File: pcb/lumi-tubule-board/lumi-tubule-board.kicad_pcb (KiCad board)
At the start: 2 copper layers, 66 parts, among them Q1 DMN1045UFR4, SW1 SWITCH_TACT_SMT4.6X2.8, SW2 SWITCH_TACT_SMT4.6X2.8, U1 SHTC3, U2 VREG_SOT23-5, U3 ESP32-S3-MINI-1, X1 USB_C

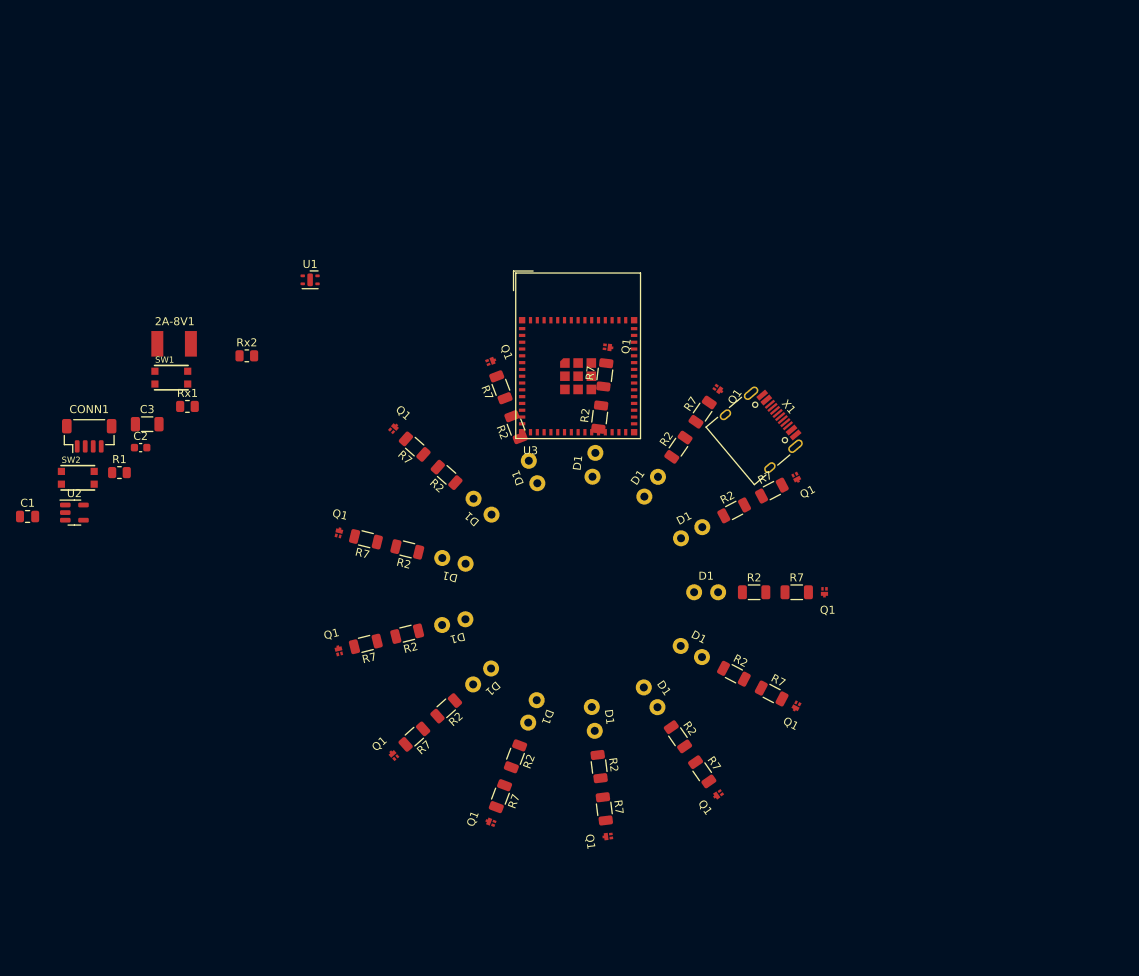
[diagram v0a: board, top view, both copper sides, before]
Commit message: PCB design update
Added LIS2DH12 accelerometer to PCB. Reworked the filament pads. Fixed footprints. Added pullup resistors to I2C lines. Started planning the layout in more compact footprint.
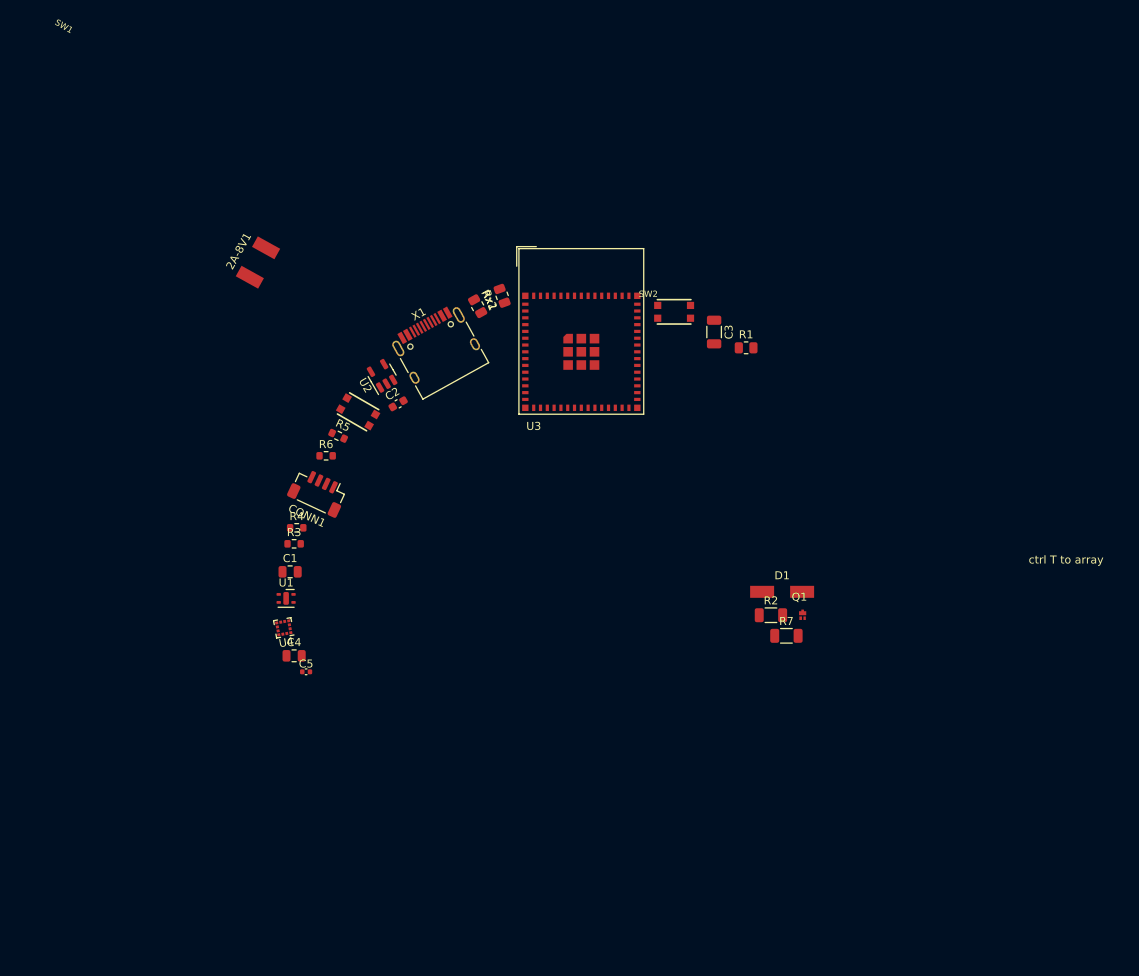
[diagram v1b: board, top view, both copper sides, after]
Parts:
- removed the D1 at (138.0, 110.6)
- removed the D1 at (166.0, 100.1)
- removed the D1 at (134.5, 96.1)
- removed the D1 at (159.1, 86.9)
- removed the D1 at (164.2, 107.5)
- removed the D1 at (164.2, 92.6)
- removed the D1 at (134.5, 103.8)
- removed the D1 at (138.1, 89.4)
- removed the D1 at (144.3, 114.9)
- removed the D1 at (151.9, 115.9)
- removed the D1 at (152.0, 84.1)
- removed the D1 at (144.4, 85.0)
- removed the D1 at (159.1, 113.2)
- removed the Q1 at (126.9, 79.6)
- removed the Q1 at (177.3, 85.7)
- removed the Q1 at (139.1, 71.2)
- removed the Q1 at (139.1, 128.8)
- removed the Q1 at (120.1, 107.4)
- removed the Q1 at (177.3, 114.3)
- removed the Q1 at (153.8, 130.6)
- removed the Q1 at (167.5, 74.7)
- removed the Q1 at (120.1, 92.7)
- removed the Q1 at (153.7, 69.4)
- removed the Q1 at (167.5, 125.3)
- removed the Q1 at (127.0, 120.4)
- removed the Q1 at (180.8, 100.0)
- removed the R2 at (172.0, 100.1)
- removed the R2 at (142.2, 79.4)
- removed the R2 at (128.6, 105.2)
- removed the R2 at (152.6, 121.8)
- removed the R2 at (162.5, 81.9)
- removed the R2 at (133.5, 114.6)
- removed the R2 at (152.7, 78.2)
- removed the R2 at (133.6, 85.4)
- removed the R2 at (142.2, 120.6)
- removed the R2 at (162.5, 118.1)
- removed the R2 at (169.5, 89.8)
- removed the R2 at (128.6, 94.7)
- removed the R2 at (169.5, 110.2)
- removed the R7 at (174.2, 112.7)
- removed the R7 at (129.6, 81.9)
- removed the R7 at (140.3, 74.4)
- removed the R7 at (140.3, 125.5)
- removed the R7 at (165.5, 122.5)
- removed the R7 at (153.3, 72.9)
- removed the R7 at (153.3, 127.1)
- removed the R7 at (177.3, 100.1)
- removed the R7 at (123.5, 106.5)
- removed the R7 at (174.2, 87.3)
- removed the R7 at (129.5, 118.1)
- removed the R7 at (123.5, 93.4)
- removed the R7 at (165.6, 77.5)
- added C4: 10uF, Capacitor_SMD:C_0805_2012Metric, F.Cu at (114.5, 108.0)
- added C5: 100nF, Capacitor_SMD:C_0402_1005Metric, F.Cu at (116.0, 110.0)
- added D1: flexible-led-filament, lumi-tubule-board:Flexible LED filament viamount, F.Cu at (175.5, 100.0)
- added Q1: DMN1045UFR4, lumi-tubule-board:DMN1045UFR4, F.Cu at (178.1, 102.9)
- added R2: 10k, Resistor_SMD:R_1206_3216Metric, F.Cu at (174.1, 102.9)
- added R3: 4.7K, Resistor_SMD:R_0603_1608Metric, F.Cu at (114.5, 94.0)
- added R4: 4.7K, Resistor_SMD:R_0603_1608Metric, F.Cu at (114.8, 92.0)
- added R5: 4.7K, Resistor_SMD:R_0603_1608Metric, F.Cu at (120.0, 80.5)
- added R6: 4.7K, Resistor_SMD:R_0603_1608Metric, F.Cu at (118.5, 83.0)
- added R7: 18, Resistor_SMD:R_1206_3216Metric, F.Cu at (176.0, 105.5)
- added U4: LIS2Dx12, Package_LGA:LGA-12_2x2mm_P0.5mm, F.Cu at (113.2, 104.5)
- moved R1 79.9 mm to (171.0, 69.5)
- moved SW2 77.4 mm to (162.0, 65.0)
- moved C3 71.8 mm to (167.0, 67.5), turned to -90 degrees
- moved U2 42.1 mm to (125.5, 73.0), turned to 120 degrees
- moved Rx1 41.7 mm to (140.5, 63.0), turned to 110 degrees
- moved X1 40.5 mm to (132.8, 70.2), turned to 29 degrees
- moved U1 39.9 mm to (113.5, 100.8)
- moved C1 33.5 mm to (114.0, 97.5)
- moved C2 32.6 mm to (127.5, 76.5), turned to 30 degrees
- moved Rx2 29.5 mm to (137.4, 64.3), turned to -61 degrees
- moved CONN1 29.5 mm to (117.5, 87.5), turned to 155 degrees
- moved SW1 23.7 mm to (122.5, 77.5), turned to -30 degrees
- moved 2A-8V1 14.6 mm to (110.0, 58.8), turned to 61 degrees
- moved U3 3.08 mm to (150.4, 67.5)
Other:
- board text added: "ctrl T to array"

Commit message: First wiring for PCB
First fully wired up arrangement for PCB. It's not pretty and the differential pairs are not good yet and the schematic still needs updating.
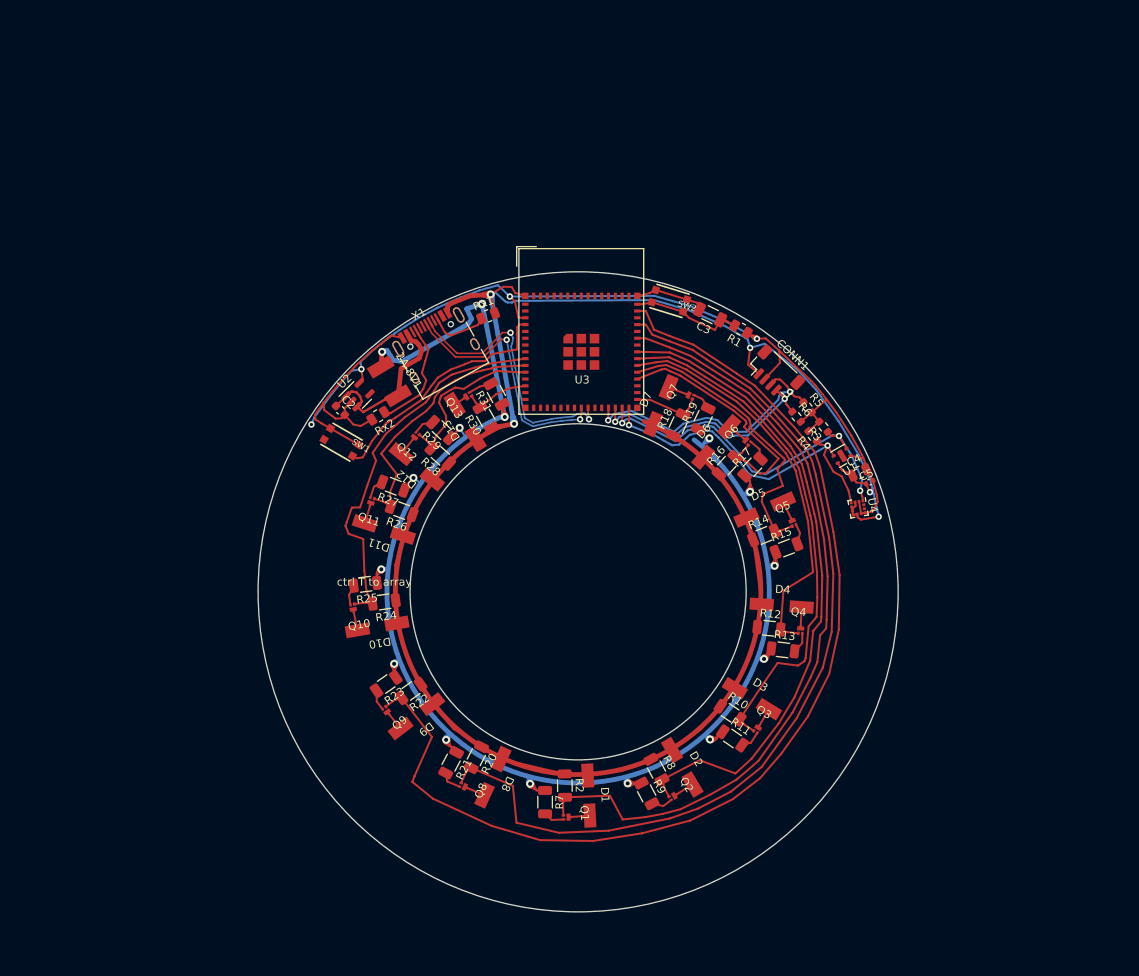
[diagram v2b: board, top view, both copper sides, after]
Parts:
- removed C1: 100nF, Capacitor_SMD:C_0805_2012Metric
- added D10: flexible-led-filament, lumi-tubule-board:Flexible LED filament viamount, F.Cu at (124.9, 104.4)
- added D11: flexible-led-filament, lumi-tubule-board:Flexible LED filament viamount, F.Cu at (125.7, 92.2)
- added D12: flexible-led-filament, lumi-tubule-board:Flexible LED filament viamount, F.Cu at (129.8, 84.4)
- added D13: flexible-led-filament, lumi-tubule-board:Flexible LED filament viamount, F.Cu at (135.9, 78.8)
- added D2: flexible-led-filament, lumi-tubule-board:Flexible LED filament viamount, F.Cu at (163.0, 121.9)
- added D3: flexible-led-filament, lumi-tubule-board:Flexible LED filament viamount, F.Cu at (171.7, 113.4)
- added D4: flexible-led-filament, lumi-tubule-board:Flexible LED filament viamount, F.Cu at (175.4, 101.7)
- added D5: flexible-led-filament, lumi-tubule-board:Flexible LED filament viamount, F.Cu at (173.3, 89.7)
- added D6: flexible-led-filament, lumi-tubule-board:Flexible LED filament viamount, F.Cu at (167.3, 81.3)
- added D7: flexible-led-filament, lumi-tubule-board:Flexible LED filament viamount, F.Cu at (160.3, 76.7)
- added D8: flexible-led-filament, lumi-tubule-board:Flexible LED filament viamount, F.Cu at (139.3, 123.2)
- added D9: flexible-led-filament, lumi-tubule-board:Flexible LED filament viamount, F.Cu at (129.8, 115.6)
- added Q10: DMN1045UFR4, lumi-tubule-board:DMN1045UFR4, F.Cu at (121.9, 101.9)
- added Q11: DMN1045UFR4, lumi-tubule-board:DMN1045UFR4, F.Cu at (124.2, 88.6)
- added Q12: DMN1045UFR4, lumi-tubule-board:DMN1045UFR4, F.Cu at (129.7, 80.5)
- added Q13: DMN1045UFR4, lumi-tubule-board:DMN1045UFR4, F.Cu at (136.2, 75.5)
- added Q2: DMN1045UFR4, lumi-tubule-board:DMN1045UFR4, F.Cu at (161.8, 125.6)
- added Q3: DMN1045UFR4, lumi-tubule-board:DMN1045UFR4, F.Cu at (172.4, 117.2)
- added Q4: DMN1045UFR4, lumi-tubule-board:DMN1045UFR4, F.Cu at (177.8, 104.8)
- added Q5: DMN1045UFR4, lumi-tubule-board:DMN1045UFR4, F.Cu at (176.9, 91.4)
- added Q6: DMN1045UFR4, lumi-tubule-board:DMN1045UFR4, F.Cu at (171.2, 81.2)
- added Q7: DMN1045UFR4, lumi-tubule-board:DMN1045UFR4, F.Cu at (164.0, 75.5)
- added Q8: DMN1045UFR4, lumi-tubule-board:DMN1045UFR4, F.Cu at (135.6, 124.3)
- added Q9: DMN1045UFR4, lumi-tubule-board:DMN1045UFR4, F.Cu at (126.0, 114.8)
- added R10: 10k, Resistor_SMD:R_1206_3216Metric, F.Cu at (169.0, 115.1)
- added R11: 18, Resistor_SMD:R_1206_3216Metric, F.Cu at (169.3, 118.3)
- added R12: 10k, Resistor_SMD:R_1206_3216Metric, F.Cu at (173.8, 104.6)
- added R13: 18, Resistor_SMD:R_1206_3216Metric, F.Cu at (175.6, 107.3)
- added R14: 10k, Resistor_SMD:R_1206_3216Metric, F.Cu at (173.2, 92.9)
- added R15: 18, Resistor_SMD:R_1206_3216Metric, F.Cu at (176.0, 94.5)
- added R16: 10k, Resistor_SMD:R_1206_3216Metric, F.Cu at (168.6, 84.2)
- added R17: 18, Resistor_SMD:R_1206_3216Metric, F.Cu at (171.8, 84.4)
- added R18: 10k, Resistor_SMD:R_1206_3216Metric, F.Cu at (162.5, 79.2)
- added R19: 18, Resistor_SMD:R_1206_3216Metric, F.Cu at (165.6, 78.4)
- added R20: 10k, Resistor_SMD:R_1206_3216Metric, F.Cu at (137.3, 120.7)
- added R21: 18, Resistor_SMD:R_1206_3216Metric, F.Cu at (134.1, 121.4)
- added R22: 10k, Resistor_SMD:R_1206_3216Metric, F.Cu at (129.1, 112.4)
- added R23: 18, Resistor_SMD:R_1206_3216Metric, F.Cu at (126.0, 111.5)
- added R24: 10k, Resistor_SMD:R_1206_3216Metric, F.Cu at (125.8, 101.3)
- added R25: 18, Resistor_SMD:R_1206_3216Metric, F.Cu at (123.4, 99.1)
- added R26: 10k, Resistor_SMD:R_1206_3216Metric, F.Cu at (127.9, 89.8)
- added R27: 18, Resistor_SMD:R_1206_3216Metric, F.Cu at (126.9, 86.8)
- added R28: 10k, Resistor_SMD:R_1206_3216Metric, F.Cu at (132.8, 83.0)
- added R29: 18, Resistor_SMD:R_1206_3216Metric, F.Cu at (132.9, 79.8)
- added R30: 10k, Resistor_SMD:R_1206_3216Metric, F.Cu at (138.5, 78.2)
- added R31: 18, Resistor_SMD:R_1206_3216Metric, F.Cu at (139.8, 75.3)
- added R8: 10k, Resistor_SMD:R_1206_3216Metric, F.Cu at (159.8, 122.2)
- added R9: 18, Resistor_SMD:R_1206_3216Metric, F.Cu at (158.6, 125.2)
- moved C5 74.3 mm to (186.4, 86.3), turned to 24 degrees
- moved C4 74.3 mm to (185.2, 85.1), turned to 24 degrees
- moved U4 73.3 mm to (185.0, 89.5), turned to -80 degrees
- moved U1 71.7 mm to (183.0, 83.0), turned to -150 degrees
- moved R3 67.8 mm to (180.7, 79.4), turned to 130 degrees
- moved R4 65.5 mm to (179.3, 80.5), turned to 130 degrees
- moved R6 59.0 mm to (177.3, 78.1), turned to -50 degrees
- moved CONN1 58.9 mm to (174.6, 72.8), turned to -43 degrees
- moved R5 58.8 mm to (178.7, 76.9), turned to -51 degrees
- moved Q1 38.8 mm to (148.5, 128.2), turned to 93 degrees
- moved R7 36.6 mm to (145.9, 126.3), turned to -90 degrees
- moved D1 35.1 mm to (151.3, 125.5), turned to -87 degrees
- moved R2 33.4 mm to (148.3, 124.2), turned to -89 degrees
- moved 2A-8V1 22.2 mm to (126.4, 73.7), turned to -59 degrees
- moved Rx2 18.5 mm to (125.0, 78.0), turned to -149 degrees
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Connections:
- CONN1 pad 1: unconnected-(CONN1-Pad1) -> GND
- CONN1 pad 2: unconnected-(CONN1-Pad2) -> /3.3V
- CONN1 pad 3: unconnected-(CONN1-Pad3) -> SDA
- CONN1 pad 4: unconnected-(CONN1-Pad4) -> SCL
- Q1 pad 2: L1 -> L7
- R2 pad 2: L1 -> L7
- U3 pad 10: L6 -> L11
- U3 pad 11: L7 -> L12
- U3 pad 12: L8 -> (no net)
- U3 pad 13: L9 -> L13
- U3 pad 14: L10 -> (no net)
- U3 pad 15: L11 -> (no net)
- U3 pad 16: L12 -> (no net)
- U3 pad 17: L13 -> (no net)
- U3 pad 27: SDA_int -> SDA
- U3 pad 28: unconnected-(U3-Pad28) -> SCL
- U3 pad 29: unconnected-(U3-Pad29) -> SCL_int
- U3 pad 30: SCL_int -> SDA_int
- U3 pad 31: unconnected-(U3-Pad31) -> L1
- U3 pad 32: unconnected-(U3-Pad32) -> (no net)
- U3 pad 33: unconnected-(U3-Pad33) -> (no net)
- U3 pad 34: unconnected-(U3-Pad34) -> L2
- U3 pad 35: unconnected-(U3-Pad35) -> L3
- U3 pad 36: unconnected-(U3-Pad36) -> L4
- U3 pad 37: unconnected-(U3-Pad37) -> L5
- U3 pad 38: unconnected-(U3-Pad38) -> L6
- U3 pad 39: unconnected-(U3-Pad39) -> (no net)
- U3 pad 40: unconnected-(U3-Pad40) -> L7
- U3 pad 42: Net-(U3-Pad1) -> L8
- U3 pad 44: unconnected-(U3-Pad44) -> L9
- U3 pad 5: L1 -> (no net)
- U3 pad 6: L2 -> (no net)
- U3 pad 62: Net-(U3-Pad1) -> GND
- U3 pad 65: Net-(U3-Pad1) -> GND
- U3 pad 7: L3 -> (no net)
- U3 pad 8: L4 -> (no net)
- U3 pad 9: L5 -> L10
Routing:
- net GND: track 0.00 -> 277.6 mm, vias 0 -> 5
- net 5V-fused: track 0.00 -> 193.5 mm, vias 0 -> 15
- net L9: track 0.00 -> 135.1 mm
- net /3.3V: track 0.00 -> 116.0 mm, vias 0 -> 4
- net L8: track 0.00 -> 114.8 mm
- net L7: track 0.00 -> 97.2 mm
- net L6: track 0.00 -> 80.7 mm
- net L5: track 0.00 -> 64.8 mm
- net L4: track 0.00 -> 49.7 mm
- net L10: track 0.00 -> 47.8 mm
- net SCL_int: track 0.00 -> 46.8 mm, vias 0 -> 3
- net SDA_int: track 0.00 -> 43.2 mm, vias 0 -> 2
- net L3: track 0.00 -> 37.0 mm
- net SDA: track 0.00 -> 34.3 mm, vias 0 -> 2
- net Net-(Q1-Pad3): track 0.00 -> 34.1 mm
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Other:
- board outline added: 80 x 80 mm
